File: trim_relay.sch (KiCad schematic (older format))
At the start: 31 parts, among them J1 Conn_01x08, J2 Conn_01x01, J3 Conn_01x01, J4 Conn_01x01, J5 Conn_01x01, K1 G5Q-1, K2 G5Q-1, K3 G5Q-1, K4 G5Q-1, K5 G5Q-1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

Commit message: pcb completed
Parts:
- removed J1: Conn_01x08, symbol Conn_01x08
- removed K1, K2, K3, K4, K5: G5Q-1, Relays_THT:Relay_SPDT_OMRON-G5Q, symbol G5Q-1
- added J10, J11, J5, J6, J7, J8, J9: Conn_01x01, CustomComponents:FASTON-187-vert-90deg-terminal, symbol Conn_01x01
- added K1, K2, K3, K4, K5: G5LE, Relays_THT:Relay_SPDT_OMRON-G5LE-1, symbol G5LE
- D1, D2, D3, D4, D5: footprint Diodes_THT:D_DO-41_SOD81_P7.62mm_Horizontal -> Diodes_THT:D_DO-41_SOD81_P10.16mm_Horizontal
- J1: renamed from J2; footprint (none) -> CustomComponents:FASTON-187-vert-90deg-terminal
- J2: renamed from J3; footprint (none) -> CustomComponents:FASTON-187-vert-90deg-terminal
- J3: renamed from J4; footprint (none) -> CustomComponents:FASTON-187-vert-90deg-terminal
- J4: renamed from J5; footprint (none) -> CustomComponents:FASTON-187-vert-90deg-terminal
- R1, R2, R3, R4, R5, R6, R7: footprint Resistors_THT:R_Axial_DIN0414_L11.9mm_D4.5mm_P15.24mm_Horizontal -> Resistors_THT:R_Axial_DIN0207_L6.3mm_D2.5mm_P10.16mm_Horizontal
- U1: footprint TO_SOT_Packages_THT:TO-92_Inline_Narrow_Oval -> TO_SOT_Packages_THT:TO-92_Horizontal2_Inline_Narrow_Oval
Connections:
- wire segments 109 -> 113
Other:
- moved on the sheet: C1, C2, J1, J2, J3, J4, Q1, R1, R2, R7, RV1, U1

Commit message: Changed all inputs to grounding for active
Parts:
- removed Q2, Q3, Q4, Q5: 2N3904, TO_SOT_Packages_THT:TO-92_Molded_Narrow, symbol 2N3904
- added Q2, Q3, Q4, Q5: 2N3906, TO_SOT_Packages_THT:TO-92_Molded_Narrow, symbol 2N3906
- added R10, R11, R8, R9: R, Resistors_THT:R_Axial_DIN0207_L6.3mm_D2.5mm_P10.16mm_Horizontal, symbol R
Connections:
- wire segments 113 -> 117
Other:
- moved on the sheet: C1, C2, R7, RV1, U1

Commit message: Fixed layout
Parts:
- removed K1, K2, K3, K4, K5: G5LE, Relays_THT:Relay_SPDT_OMRON-G5LE-1, symbol G5LE
- added K1, K2, K3, K4, K5: G5Q-14 DC12, Relays_THT:Relay_SPDT_OMRON-G5Q, symbol G5Q-1
- C1, C2: value CP -> 0.68uF
- Q1, Q2, Q3, Q4, Q5: footprint TO_SOT_Packages_THT:TO-92_Molded_Narrow -> TO_SOT_Packages_THT:TO-92_Inline_Wide
- R1, R10, R11, R8, R9: value R -> 10K
- R2, R3, R4, R5, R6: value R -> 3K9
- R7: value R -> 120
- RV1: value POT -> 1K
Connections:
- wire segments 117 -> 115

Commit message: Switch 1 power supply to 1 for each system
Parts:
- added J10: Conn_01x01, CustomComponents:FASTON-187-vert-90deg-terminal, symbol Conn_01x01
- renumbered J10 to J11, J11 to J12
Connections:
- net +12V renamed VDD
- net VDD: no longer K2.3, K3.3, Q2.1 (E), Q3.1 (E), R8.1, R9.1
- new net VCC: J10.1 (Pin_1), K2.3, K3.3, Q2.1 (E), Q3.1 (E), R8.1, R9.1
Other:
- note added: "POWER-AILERON"
- note added: "POWER-ELEVATOR"
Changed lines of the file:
@@
-	1    0    0    -1
-$EndComp
-$Comp
-L +12V #PWR01
-U 1 1 5B5AA76E
-P 2250 2650
-F 0 "#PWR01" H 2250 2500 50  0001 C CNN
-F 1 "+12V" H 2250 2790 50  0000 C CNN
-F 2 "" H 2250 2650 50  0001 C CNN
-F 3 "" H 2250 2650 50  0001 C CNN
-	1    2250 2650
 	1    0    0    -1
 $EndComp
@@
 	2550 1000 2550 1100
 $Comp
-L GND #PWR02
+L GND #PWR01
 U 1 1 5B5AA7E6
 P 1900 1000
-F 0 "#PWR02" H 1900 750 50  0001 C CNN
+F 0 "#PWR01" H 1900 750 50  0001 C CNN
 F 1 "GND" H 1900 850 50  0000 C CNN
 F 2 "" H 1900 1000 50  0001 C CNN
@@
 Wire Wire Line
 	3200 4600 3200 4700
-$Comp
-L +12V #PWR03
-U 1 1 5B5AC33F
-P 3850 2750
-F 0 "#PWR03" H 3850 2600 50  0001 C CNN
-F 1 "+12V" H 3850 2890 50  0000 C CNN
-F 2 "" H 3850 2750 50  0001 C CNN
-F 3 "" H 3850 2750 50  0001 C CNN
-	1    3850 2750
-	1    0    0    -1
-$EndComp
 Connection ~ 3850 2850
 Connection ~ 3000 2950
@@
 Connection ~ 2050 2650
 $Comp
-L +12V #PWR04
-U 1 1 5B5AD418
-P 2400 6500
-F 0 "#PWR04" H 2400 6350 50  0001 C CNN
-F 1 "+12V" H 2400 6640 50  0000 C CNN
-F 2 "" H 2400 6500 50  0001 C CNN
-F 3 "" H 2400 6500 50  0001 C CNN
-	1    2400 6500
-	1    0    0    -1
-$EndComp
-$Comp
-L GND #PWR05
+L GND #PWR02
 U 1 1 5B5AD638
 P 2000 4500
-F 0 "#PWR05" H 2000 4250 50  0001 C CNN
+F 0 "#PWR02" H 2000 4250 50  0001 C CNN
 F 1 "GND" H 2000 4350 50  0000 C CNN
 F 2 "" H 2000 4500 50  0001 C CNN
@@
 $EndComp
 $Comp
-L GND #PWR06
+L GND #PWR03
 U 1 1 5B5AD990
 P 2000 2950
-F 0 "#PWR06" H 2000 2700 50  0001 C CNN
+F 0 "#PWR03" H 2000 2700 50  0001 C CNN
 F 1 "GND" H 2000 2800 50  0000 C CNN
 F 2 "" H 2000 2950 50  0001 C CNN
@@
 	7700 5400 7700 5250
 $Comp
-L +12V #PWR07
-U 1 1 5B5AE312
-P 7050 6400
-F 0 "#PWR07" H 7050 6250 50  0001 C CNN
-F 1 "+12V" H 7050 6540 50  0000 C CNN
-F 2 "" H 7050 6400 50  0001 C CNN
-F 3 "" H 7050 6400 50  0001 C CNN
-	1    7050 6400
-	1    0    0    -1
-$EndComp
-$Comp
-L GND #PWR08
+L GND #PWR04
 U 1 1 5B5AE318
 P 6600 2900
-F 0 "#PWR08" H 6600 2650 50  0001 C CNN
+F 0 "#PWR04" H 6600 2650 50  0001 C CNN
 F 1 "GND" H 6600 2750 50  0000 C CNN
 F 2 "" H 6600 2900 50  0001 C CNN
@@
 $EndComp
 $Comp
-L GND #PWR09
+L GND #PWR05
 U 1 1 5B5AE31E
 P 6600 4450
-F 0 "#PWR09" H 6600 4200 50  0001 C CNN
+F 0 "#PWR05" H 6600 4200 50  0001 C CNN
 F 1 "GND" H 6600 4300 50  0000 C CNN
 F 2 "" H 6600 4450 50  0001 C CNN
@@
 Connection ~ 4100 7400
 $Comp
-L GND #PWR010
+L GND #PWR06
 U 1 1 5B5AF061
 P 3400 7400
-F 0 "#PWR010" H 3400 7150 50  0001 C CNN
+F 0 "#PWR06" H 3400 7150 50  0001 C CNN
 F 1 "GND" H 3400 7250 50  0000 C CNN
 F 2 "" H 3400 7400 50  0001 C CNN
 F 3 "" H 3400 7400 50  0001 C CNN
 	1    3400 7400
-	1    0    0    -1
-$EndComp
-$Comp
-L +12V #PWR011
-U 1 1 5B5AF0D8
-P 3400 6550
-F 0 "#PWR011" H 3400 6400 50  0001 C CNN
-F 1 "+12V" H 3400 6690 50  0000 C CNN
-F 2 "" H 3400 6550 50  0001 C CNN
-F 3 "" H 3400 6550 50  0001 C CNN
-	1    3400 6550
 	1    0    0    -1
 $EndComp
@@
 Wire Wire Line
 	5200 1850 5400 1850
-$Comp
-L +12V #PWR012
-U 1 1 5B5B3953
-P 3400 950
-F 0 "#PWR012" H 3400 800 50  0001 C CNN
-F 1 "+12V" H 3400 1090 50  0000 C CNN
-F 2 "" H 3400 950 50  0001 C CNN
-F 3 "" H 3400 950 50  0001 C CNN
-	1    3400 950
-	1    0    0    -1
-$EndComp
 Text GLabel 3150 650  2    60   Input ~ 0
 V_ADJ
@@
 $EndComp
 $Comp
-L Conn_01x01 J10
+L Conn_01x01 J11
 U 1 1 5B5F9608
 P 9050 1550
-F 0 "J10" H 9050 1650 50  0000 C CNN
+F 0 "J11" H 9050 1650 50  0000 C CNN
 F 1 "Conn_01x01" H 9050 1450 50  0000 C CNN
 F 2 "CustomComponents:FASTON-187-vert-90deg-terminal" H 9050 1550 50  0001 C CNN
@@
 $EndComp
 $Comp
-L Conn_01x01 J11
+L Conn_01x01 J12
 U 1 1 5B5F960F
 P 9050 1850
-F 0 "J11" H 9050 1950 50  0000 C CNN
+F 0 "J12" H 9050 1950 50  0000 C CNN
 F 1 "Conn_01x01" H 9050 1750 50  0000 C CNN
 F 2 "CustomComponents:FASTON-187-vert-90deg-terminal" H 9050 1850 50  0001 C CNN
@@
 	8650 1850 8850 1850
 $Comp
-L +12V #PWR013
-U 1 1 5B5FD493
-P 8650 1550
-F 0 "#PWR013" H 8650 1400 50  0001 C CNN
-F 1 "+12V" H 8650 1690 50  0000 C CNN
-F 2 "" H 8650 1550 50  0001 C CNN
-F 3 "" H 8650 1550 50  0001 C CNN
-	1    8650 1550
-	1    0    0    -1
-$EndComp
-$Comp
-L GND #PWR014
+L GND #PWR07
 U 1 1 5B5FD5D6
 P 8650 1850
-F 0 "#PWR014" H 8650 1600 50  0001 C CNN
+F 0 "#PWR07" H 8650 1600 50  0001 C CNN
 F 1 "GND" H 8650 1700 50  0000 C CNN
 F 2 "" H 8650 1850 50  0001 C CNN
@@
 Wire Wire Line
 	7300 3700 7300 3650
+$Comp
+L Conn_01x01 J10
+U 1 1 5B65EFF7
+P 9050 1250
+F 0 "J10" H 9050 1350 50  0000 C CNN
+F 1 "Conn_01x01" H 9050 1150 50  0000 C CNN
+F 2 "CustomComponents:FASTON-187-vert-90deg-terminal" H 9050 1250 50  0001 C CNN
+F 3 "" H 9050 1250 50  0001 C CNN
+	1    9050 1250
+	1    0    0    -1
+$EndComp
+$Comp
+L VCC #PWR08
+U 1 1 5B65F2C6
+P 8650 1250
+F 0 "#PWR08" H 8650 1100 50  0001 C CNN
+F 1 "VCC" H 8650 1400 50  0000 C CNN
+F 2 "" H 8650 1250 50  0001 C CNN
+F 3 "" H 8650 1250 50  0001 C CNN
+	1    8650 1250
+	1    0    0    -1
+$EndComp
+$Comp
+L VDD #PWR09
+U 1 1 5B65F32E
+P 8650 1550
+F 0 "#PWR09" H 8650 1400 50  0001 C CNN
+F 1 "VDD" H 8650 1700 50  0000 C CNN
+F 2 "" H 8650 1550 50  0001 C CNN
+F 3 "" H 8650 1550 50  0001 C CNN
+	1    8650 1550
+	1    0    0    -1
+$EndComp
+Wire Wire Line
+	8850 1250 8650 1250
+Text Notes 9375 1600 0    60   ~ 0
+POWER-ELEVATOR
+Text Notes 9375 1300 0    60   ~ 0
+POWER-AILERON
+$Comp
+L VDD #PWR010
+U 1 1 5B6627AC
+P 7050 6400
+F 0 "#PWR010" H 7050 6250 50  0001 C CNN
+F 1 "VDD" H 7050 6550 50  0000 C CNN
+F 2 "" H 7050 6400 50  0001 C CNN
+F 3 "" H 7050 6400 50  0001 C CNN
+	1    7050 6400
+	1    0    0    -1
+$EndComp
+$Comp
+L VDD #PWR011
+U 1 1 5B6633BC
+P 3400 6550
+F 0 "#PWR011" H 3400 6400 50  0001 C CNN
+F 1 "VDD" H 3400 6700 50  0000 C CNN
+F 2 "" H 3400 6550 50  0001 C CNN
+F 3 "" H 3400 6550 50  0001 C CNN
+	1    3400 6550
+	1    0    0    -1
+$EndComp
+$Comp
+L VCC #PWR012
+U 1 1 5B663EC5
+P 3850 2750
+F 0 "#PWR012" H 3850 2600 50  0001 C CNN
+F 1 "VCC" H 3850 2900 50  0000 C CNN
+F 2 "" H 3850 2750 50  0001 C CNN
+F 3 "" H 3850 2750 50  0001 C CNN
+	1    3850 2750
+	1    0    0    -1
+$EndComp
+$Comp
+L VCC #PWR013
+U 1 1 5B664FE0
+P 2400 6500
+F 0 "#PWR013" H 2400 6350 50  0001 C CNN
+F 1 "VCC" H 2400 6650 50  0000 C CNN
+F 2 "" H 2400 6500 50  0001 C CNN
+F 3 "" H 2400 6500 50  0001 C CNN
+	1    2400 6500
+	1    0    0    -1
+$EndComp
+$Comp
+L VDD #PWR014
+U 1 1 5B665897
+P 3400 950
+F 0 "#PWR014" H 3400 800 50  0001 C CNN
+F 1 "VDD" H 3400 1100 50  0000 C CNN
+F 2 "" H 3400 950 50  0001 C CNN
+F 3 "" H 3400 950 50  0001 C CNN
+	1    3400 950
+	1    0    0    -1
+$EndComp
+$Comp
+L VDD #PWR015
+U 1 1 5B66599E
+P 2250 2650
+F 0 "#PWR015" H 2250 2500 50  0001 C CNN
+F 1 "VDD" H 2250 2800 50  0000 C CNN
+F 2 "" H 2250 2650 50  0001 C CNN
+F 3 "" H 2250 2650 50  0001 C CNN
+	1    2250 2650
+	1    0    0    -1
+$EndComp
 $EndSCHEMATC

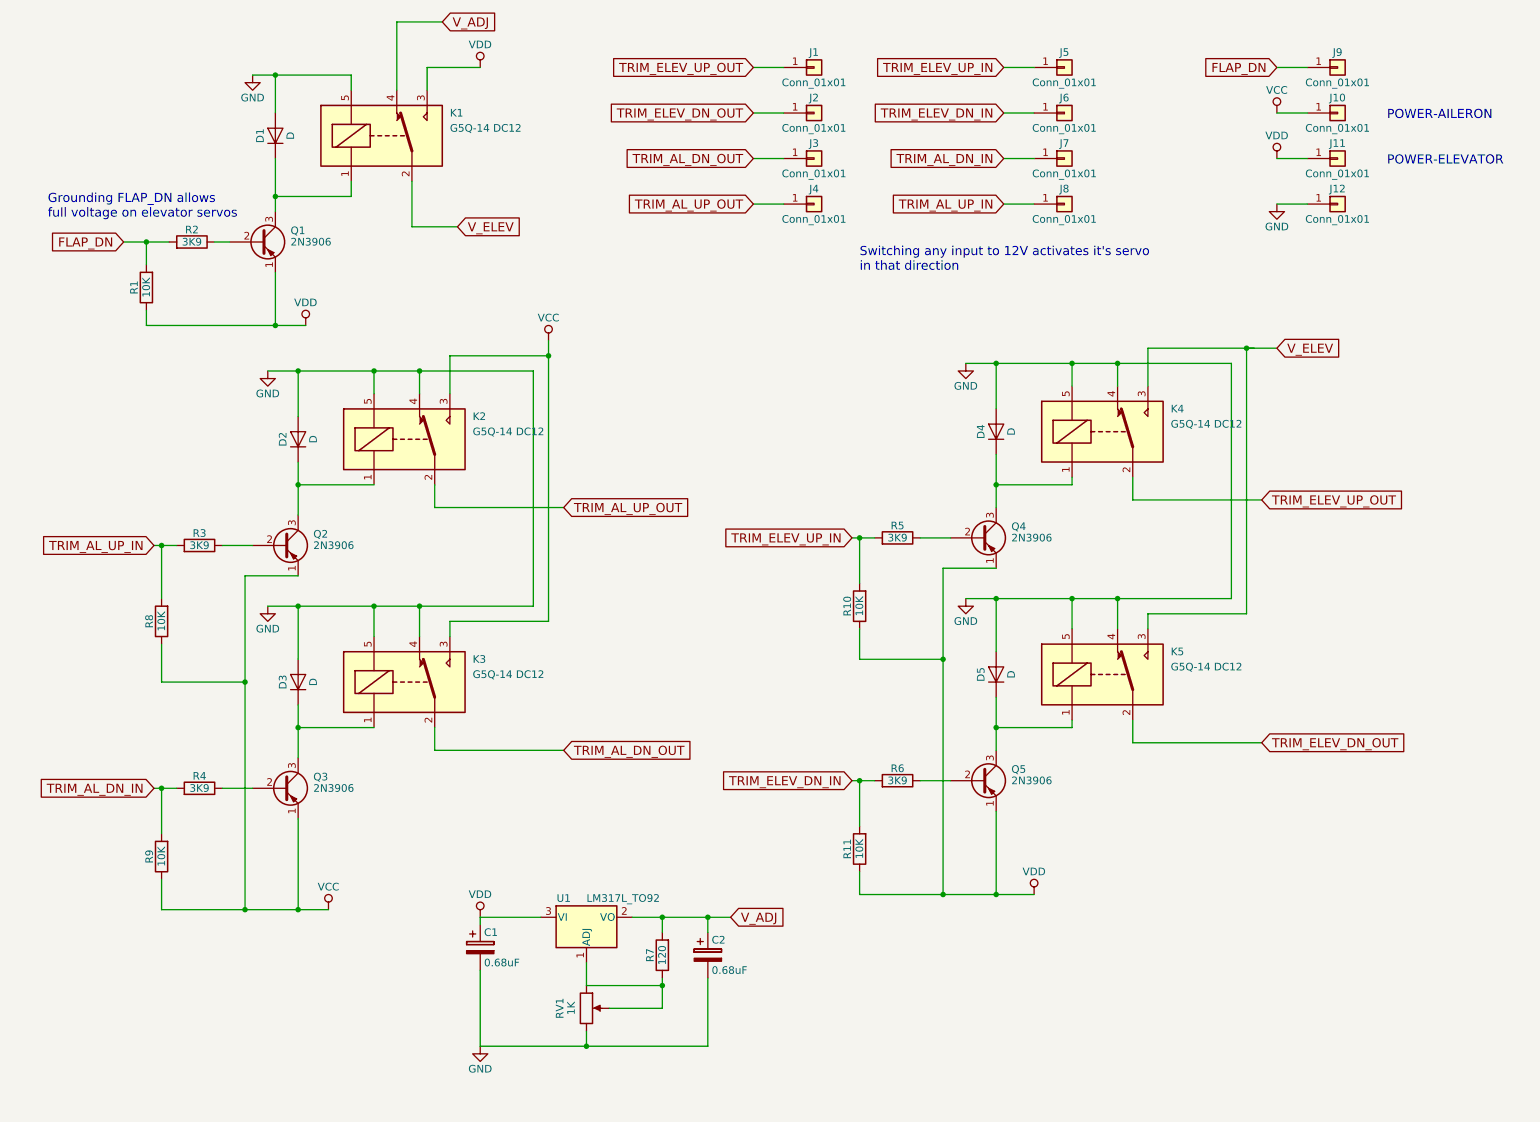
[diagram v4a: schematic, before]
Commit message: Redid schematic and pcb, removed transistors
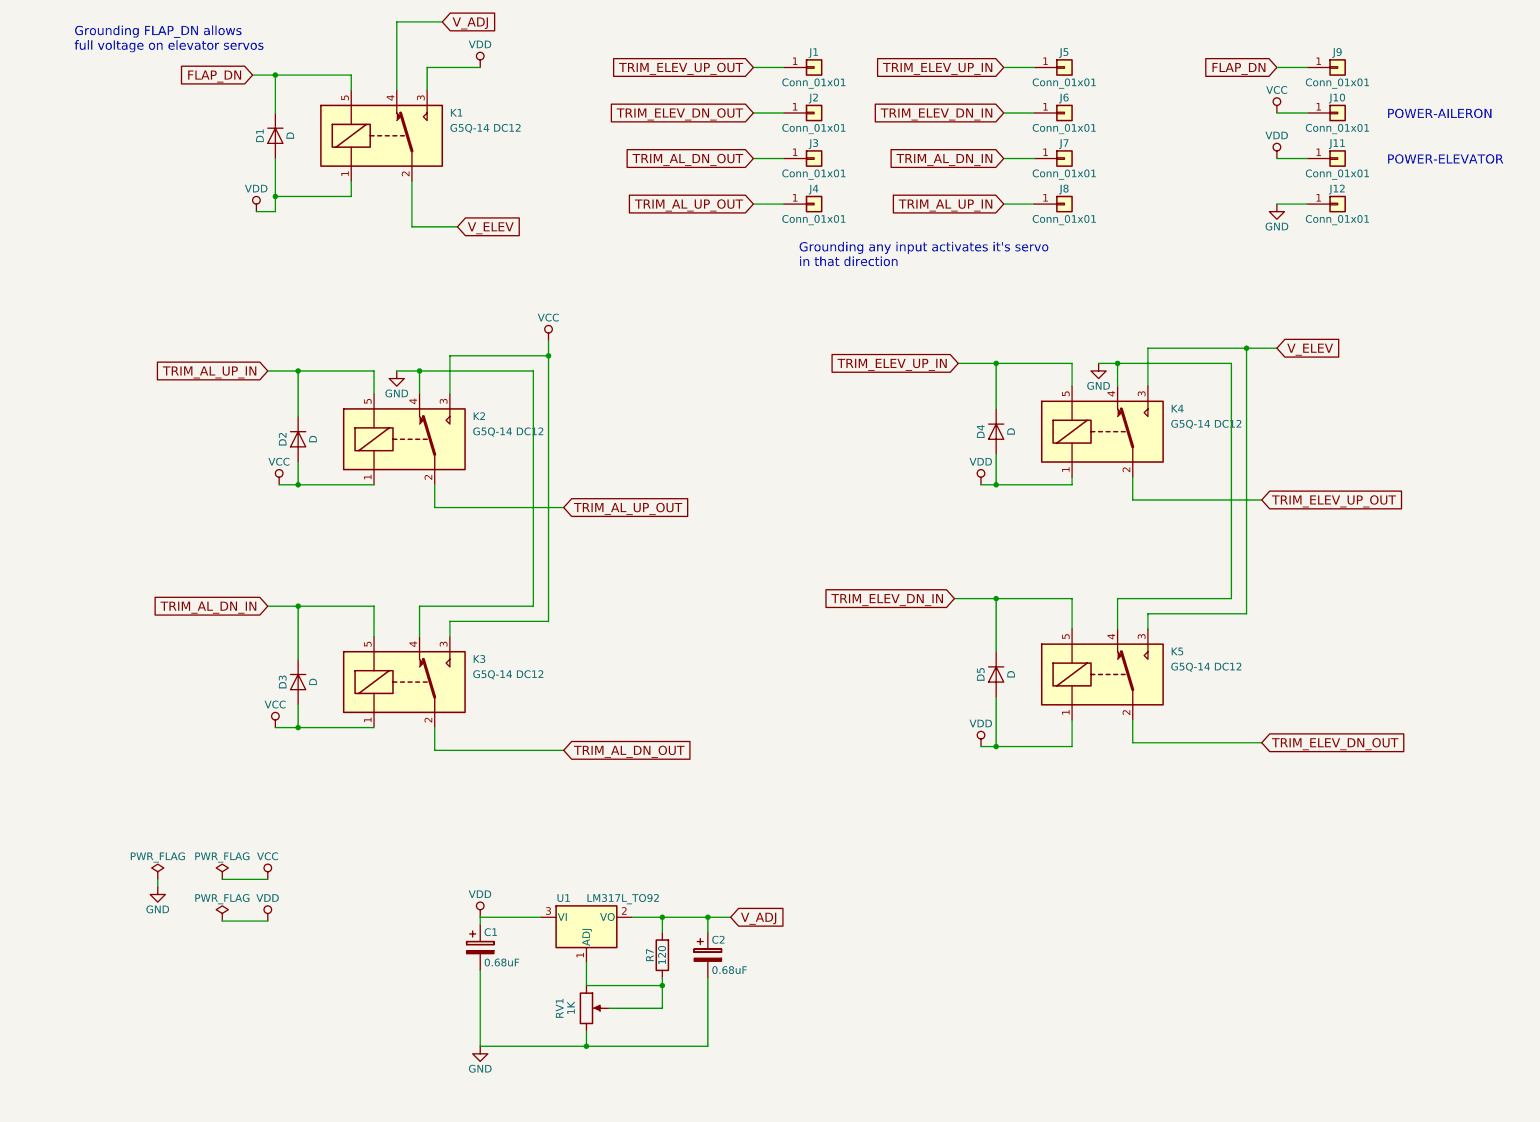
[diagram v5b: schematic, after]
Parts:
- removed Q1, Q2, Q3, Q4, Q5: 2N3906, TO_SOT_Packages_THT:TO-92_Inline_Wide, symbol 2N3906
- removed R1, R10, R11, R8, R9: 10K, Resistors_THT:R_Axial_DIN0207_L6.3mm_D2.5mm_P10.16mm_Horizontal, symbol R
- removed R2, R3, R4, R5, R6: 3K9, Resistors_THT:R_Axial_DIN0207_L6.3mm_D2.5mm_P10.16mm_Horizontal, symbol R
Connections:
- net FLAP_DN: now also D1.1 (K), K1.5
- net GND: no longer D1.2 (A), D2.2 (A), D3.2 (A), D4.2 (A), D5.2 (A), K1.5, K2.5, K3.5, K4.5, K5.5
- net TRIM_AL_DN_IN: now also D3.1 (K), K3.5
- net TRIM_AL_UP_IN: now also D2.1 (K), K2.5
- net TRIM_ELEV_DN_IN: now also D5.1 (K), K5.5
- net TRIM_ELEV_UP_IN: now also D4.1 (K), K4.5
- net VCC: now also D2.2 (A), D3.2 (A), K2.1, K3.1
- net VDD: now also D1.2 (A), D4.2 (A), D5.2 (A), K1.1, K4.1, K5.1
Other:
- note added: "Grounding any input activates it's servo\nin that direction"
- note removed: "Switching any input to 12V activates it's servo\nin that direction"
